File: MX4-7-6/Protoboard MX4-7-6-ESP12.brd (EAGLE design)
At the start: 52.8 x 59.6 mm, 52 parts

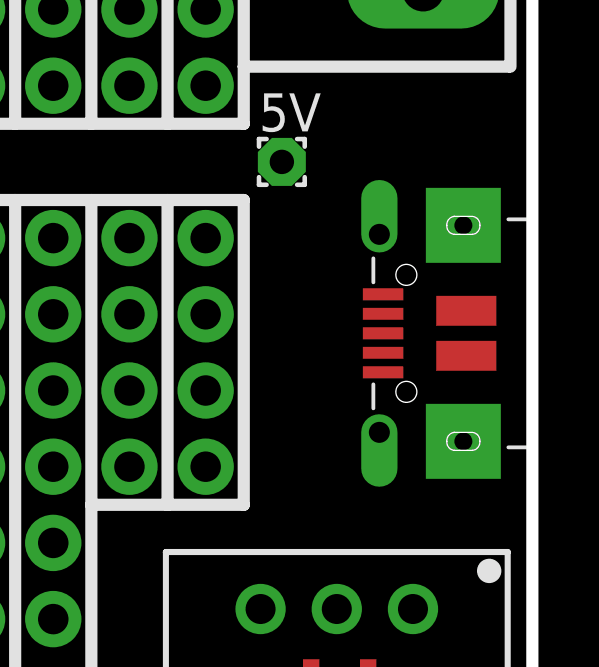
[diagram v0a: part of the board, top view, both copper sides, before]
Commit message: Change usb connector
Change to correct usb connecter and moved esp8266 bit more onto the
board.
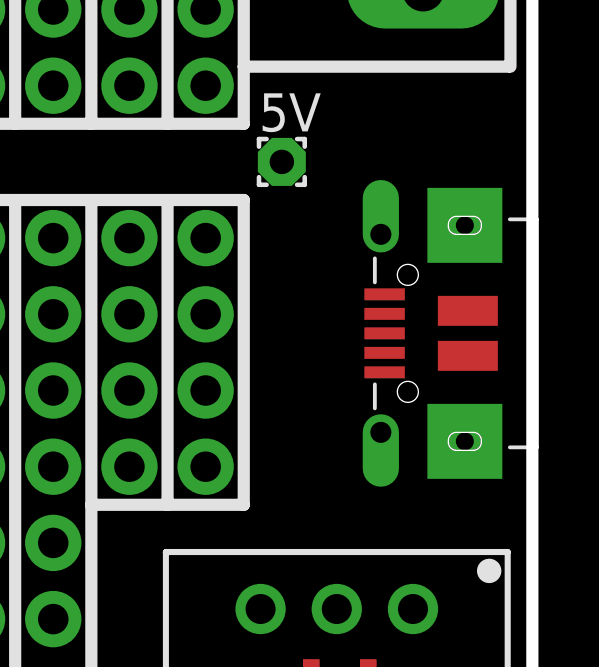
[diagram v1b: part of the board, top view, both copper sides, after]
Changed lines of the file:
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@@
 <attribute name="VALUE" x="27.445" y="25.975" size="0.6096" layer="27" rot="R200"/>
 </element>
-<element name="X2" library="microbuilder" package="4UCONN_20329" value="" x="48.6" y="25.4" smashed="yes" rot="R90">
-<attribute name="VALUE" x="55.01" y="22.622" size="0.4064" layer="27" ratio="10" rot="R90"/>
+<element name="X2" library="microbuilder" package="4UCONN_20329" value="" x="48.65" y="25.4" smashed="yes" rot="R90">
+<attribute name="VALUE" x="55.06" y="22.622" size="0.4064" layer="27" ratio="10" rot="R90"/>
 </element>
 <element name="MDL1" library="ESP8266-ESP12E" package="ESP8266-ESP12E" value="" x="13.07" y="29.39" smashed="yes" rot="R90">
@@
 <contactref element="MIC5502" pad="3"/>
 <contactref element="5V" pad="1"/>
-<wire x1="47.825" y1="24.1" x2="44.45" y2="31.115" width="0" layer="19" extent="1-1"/>
-<wire x1="48.8208625" y1="16.211459375" x2="47.825" y2="24.1" width="0" layer="19" extent="1-1"/>
+<wire x1="47.875" y1="24.1" x2="44.45" y2="31.115" width="0" layer="19" extent="1-1"/>
+<wire x1="48.8208625" y1="16.211459375" x2="47.875" y2="24.1" width="0" layer="19" extent="1-1"/>
 <wire x1="47.33" y1="11.3399" x2="48.8208625" y2="16.211459375" width="0" layer="19" extent="1-1"/>
 <wire x1="45.43" y1="11.3399" x2="47.33" y2="11.3399" width="0" layer="19" extent="1-1"/>

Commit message: Update esp component and usb
test
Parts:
- removed MDL1: (no value), ESP8266-ESP12E:ESP8266-ESP12E
- added X1: ESP-12E, microbuilder:ESP-12E
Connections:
- net GND: now also X1.9; no longer MDL1.9
- net N$10: now also X1.13; no longer MDL1.13
- net N$11: now also X1.12; no longer MDL1.12
- net N$12: now also X1.11; no longer MDL1.11
- net N$13: now also X1.10; no longer MDL1.10
- net N$26: now also X1.4; no longer MDL1.5
- net N$34: now also X1.7
- net N$50: now also X1.1; no longer MDL1.1
- net N$51: now also X1.2; no longer MDL1.2
- net N$52: now also X1.3; no longer MDL1.3
- net N$55: now also X1.5; no longer MDL1.6
- net N$56: now also X1.6; no longer MDL1.7
- net N$9: now also X1.14; no longer MDL1.14
- net RX: now also X1.15; no longer MDL1.15
- net TX: now also X1.16; no longer MDL1.16
- net VDD: now also X1.8; no longer MDL1.8

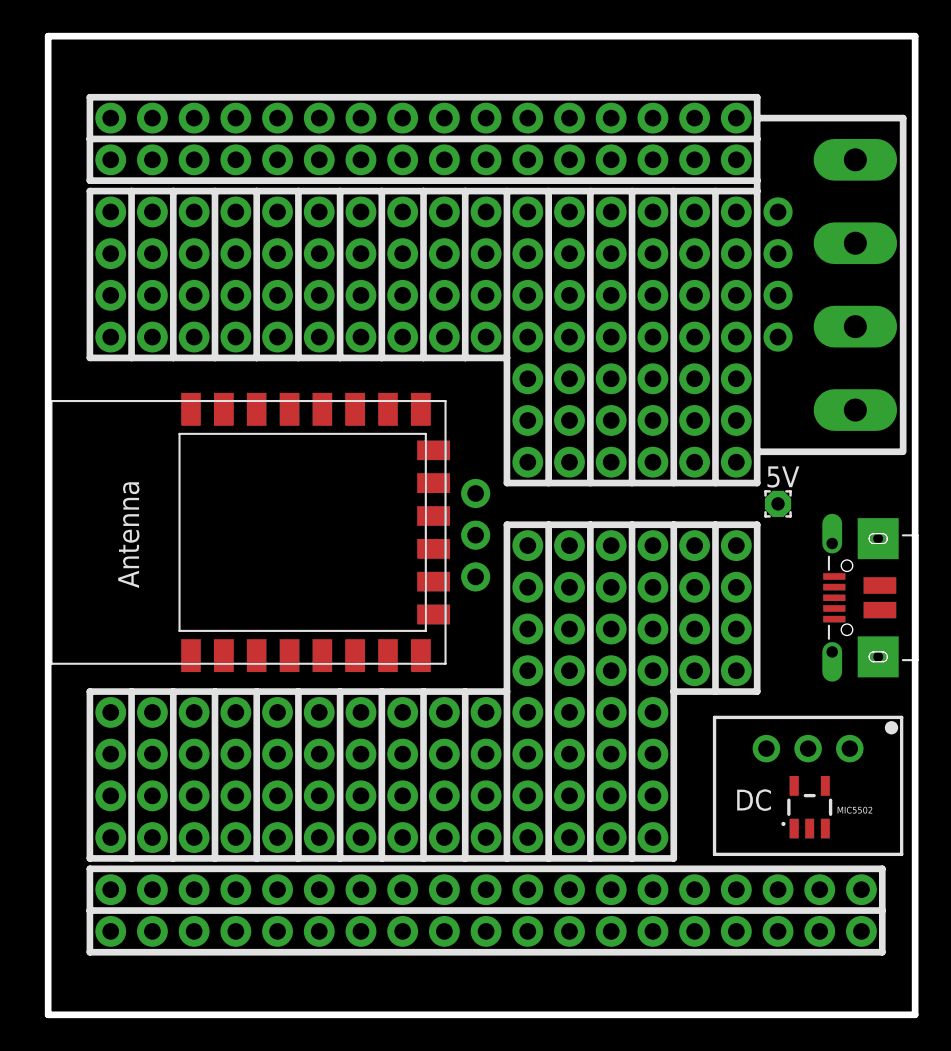
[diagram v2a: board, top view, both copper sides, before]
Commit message: Routing and Gerber files
Routed and produced gerber files
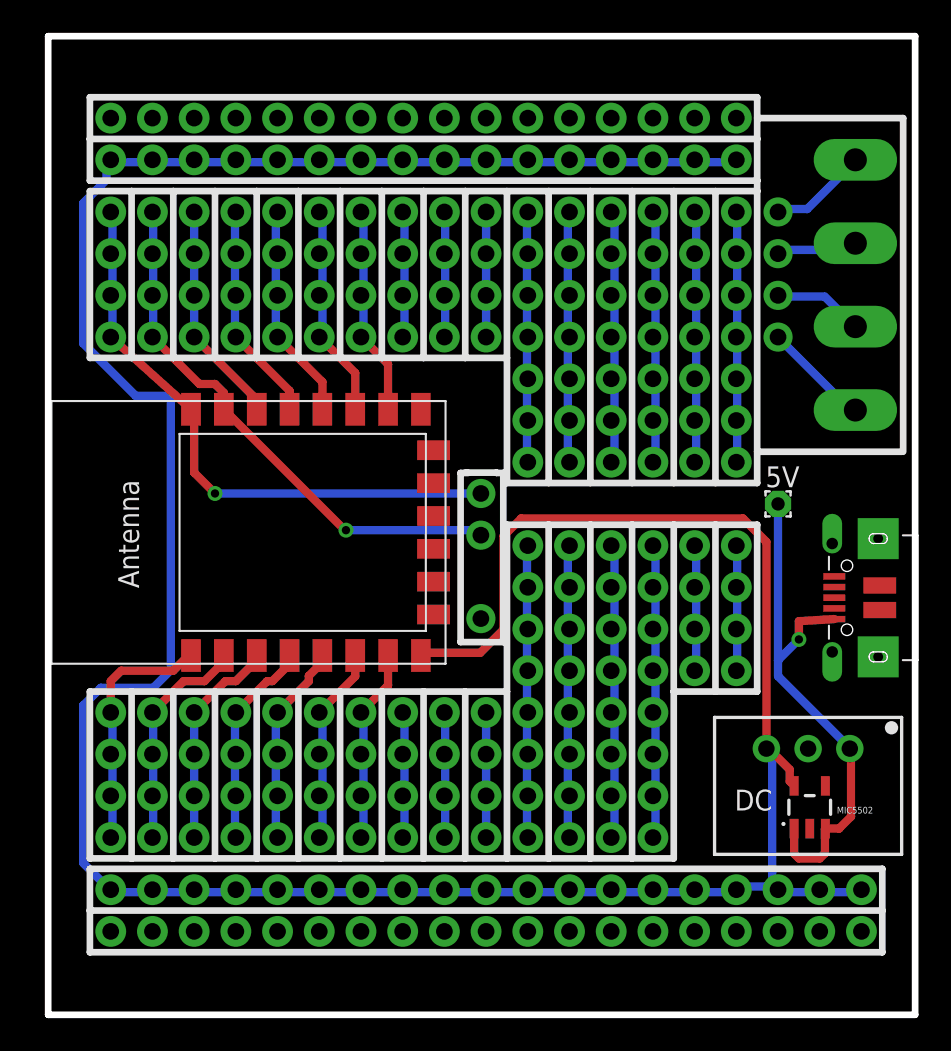
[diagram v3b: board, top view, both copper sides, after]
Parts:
- moved J1 12.7 mm to (6.35, 41.3)
- moved J8 12.7 mm to (3.81, 41.3)
- moved J6 5.08 mm to (16.5, 41.3)
- moved J3 5.08 mm to (8.89, 41.3)
- moved J4 5.08 mm to (11.4, 41.3)
- moved J5 5.08 mm to (14.0, 41.3)
- moved J7 5.08 mm to (19.1, 41.3)
- moved JP5 2.56 mm to (26.4, 24.1)
- moved JP3 0.32 mm to (26.4, 31.8)
- moved JP4 0.32 mm to (26.4, 29.2)
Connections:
- removed net N$3: J8.1, J8.2, J8.3, J8.4
- removed net N$7: J1.1, J1.2, J1.3, J1.4
- net RX: now also J1.1, J1.2, J1.3, J1.4
- net TX: now also J8.1, J8.2, J8.3, J8.4
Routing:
- net VDD: track 0.00 -> 194.8 mm
- net TX: track 0.00 -> 36.3 mm, vias 0 -> 1
- net RX: track 0.00 -> 33.5 mm, vias 0 -> 1
- net VCC: track 0.00 -> 33.0 mm, vias 0 -> 1
- net N$27: track 0.00 -> 19.2 mm
- net N$28: track 0.00 -> 18.7 mm
- net N$25: track 0.00 -> 18.3 mm
- net N$22: track 0.00 -> 17.9 mm
- net N$18: track 0.00 -> 16.5 mm
- net N$19: track 0.00 -> 16.1 mm
- net N$20: track 0.00 -> 15.7 mm
- net N$17: track 0.00 -> 15.7 mm
- net N$21: track 0.00 -> 15.4 mm
- net N$1: track 0.00 -> 15.4 mm
- net N$50: track 0.00 -> 15.2 mm
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
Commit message: Silkscreen text fixes
Silkscreen text fixes
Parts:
- moved JP3 1.27 mm to (26.4, 33.0)
- moved JP4 1.27 mm to (26.4, 30.5)
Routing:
- net RX: track 33.5 -> 34.1 mm
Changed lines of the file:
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@@
 <wire x1="52.07" y1="34.29" x2="52.07" y2="54.61" width="0.4064" layer="25"/>
 <wire x1="52.07" y1="54.61" x2="43.18" y2="54.61" width="0.4064" layer="25"/>
-<wire x1="25.4" y1="33.02" x2="27.3" y2="33.02" width="0.4064" layer="25"/>
-<wire x1="27.3" y1="33.02" x2="27.3" y2="33" width="0.4064" layer="25"/>
-<wire x1="27.3" y1="33" x2="27.7175" y2="33" width="0.4064" layer="25"/>
+<wire x1="25.4" y1="34.29" x2="27.3" y2="34.29" width="0.4064" layer="25"/>
+<wire x1="27.3" y1="34.29" x2="27.77625" y2="34.27" width="0.4064" layer="25"/>
+<wire x1="27.77625" y1="34.27" x2="27.7175" y2="33" width="0.4064" layer="25"/>
 <wire x1="27.7175" y1="33" x2="27.7175" y2="22.7" width="0.4064" layer="25"/>
 <wire x1="27.7175" y1="22.7" x2="25.1175" y2="22.7" width="0.4064" layer="25"/>
 <wire x1="25.1175" y1="22.7" x2="25.1175" y2="33" width="0.4064" layer="25"/>
-<wire x1="25.1175" y1="33" x2="25.6" y2="33" width="0.4064" layer="25"/>
+<wire x1="25.1175" y1="33" x2="25.12375" y2="34.27" width="0.4064" layer="25"/>
 </plain>
 <attributes>
@@
 <attribute name="NAME" x="41.8058625" y="12.441459375" size="1.27" layer="25"/>
 </element>
-<element name="JP3" library="adafruit" package="1X01-CLEANBIG" value="TX" x="26.3525" y="31.75" smashed="yes">
-<attribute name="VALUE" x="27.2525" y="30.805" size="0.3048" layer="27" rot="R200"/>
-</element>
-<element name="JP4" library="adafruit" package="1X01-CLEANBIG" value="RX" x="26.3525" y="29.21" smashed="yes">
-<attribute name="VALUE" x="27.2975" y="28.165" size="0.3048" layer="27" rot="R200"/>
+<element name="JP3" library="adafruit" package="1X01-CLEANBIG" value="TX" x="26.3525" y="33.02" smashed="yes">
+<attribute name="VALUE" x="27.2525" y="32.075" size="0.3048" layer="27" rot="R200"/>
+</element>
+<element name="JP4" library="adafruit" package="1X01-CLEANBIG" value="RX" x="26.3525" y="30.48" smashed="yes">
+<attribute name="VALUE" x="27.2975" y="29.435" size="0.3048" layer="27" rot="R200"/>
 </element>
 <element name="JP5" library="adafruit" package="1X01-CLEANBIG" value="GND" x="26.3525" y="24.13" smashed="yes">
@@
 <wire x1="3.9116" y1="46.5836" x2="3.81" y2="46.355" width="0.508" layer="16"/>
 <wire x1="8.7" y1="36.88" x2="3.81" y2="41.275" width="0.508" layer="1"/>
-<wire x1="26.3525" y1="31.75" x2="10.16" y2="31.75" width="0.508" layer="16"/>
+<wire x1="26.3525" y1="33.02" x2="10.16" y2="31.75" width="0.508" layer="16"/>
 <via x="10.16" y="31.75" extent="1-16" drill="0.508" shape="square"/>
 <wire x1="10.16" y1="31.75" x2="8.89" y2="33.02" width="0.508" layer="1"/>
@@
 <contactref element="J1" pad="1"/>
 <wire x1="18.1356" y1="29.5148" x2="26.3144" y2="29.5148" width="0.508" layer="16"/>
-<wire x1="26.3144" y1="29.5148" x2="26.3525" y2="29.21" width="0.508" layer="16"/>
+<wire x1="26.3144" y1="29.5148" x2="26.3525" y2="30.48" width="0.508" layer="16"/>
 <wire x1="6.4008" y1="41.2496" x2="6.35" y2="41.275" width="0.508" layer="16"/>
 <wire x1="6.4008" y1="41.6052" x2="6.4008" y2="43.7388" width="0.508" layer="16"/>
